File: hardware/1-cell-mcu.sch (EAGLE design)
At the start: 13 parts, among them IC1 PIC12LF1571, J1 ICSP_HEADER, J2 HEADER_4P, J3 HEADER_4P

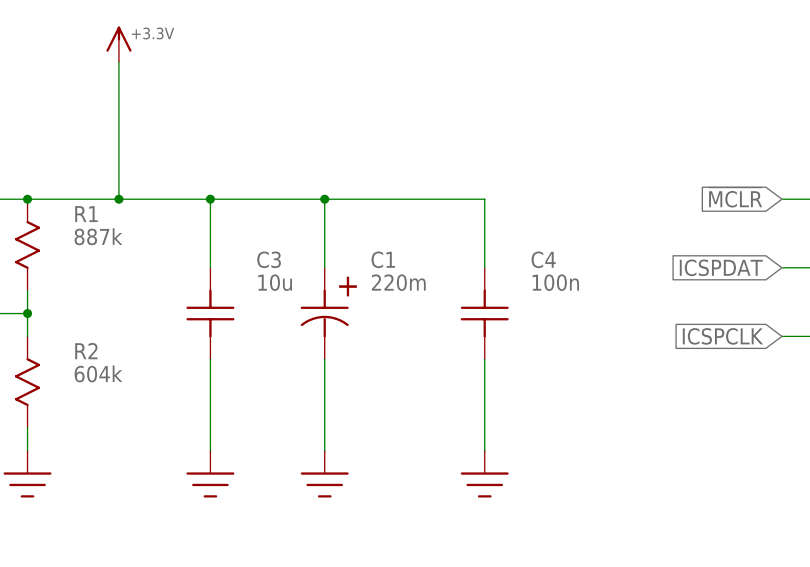
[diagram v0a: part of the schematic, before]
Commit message: updated supercap value
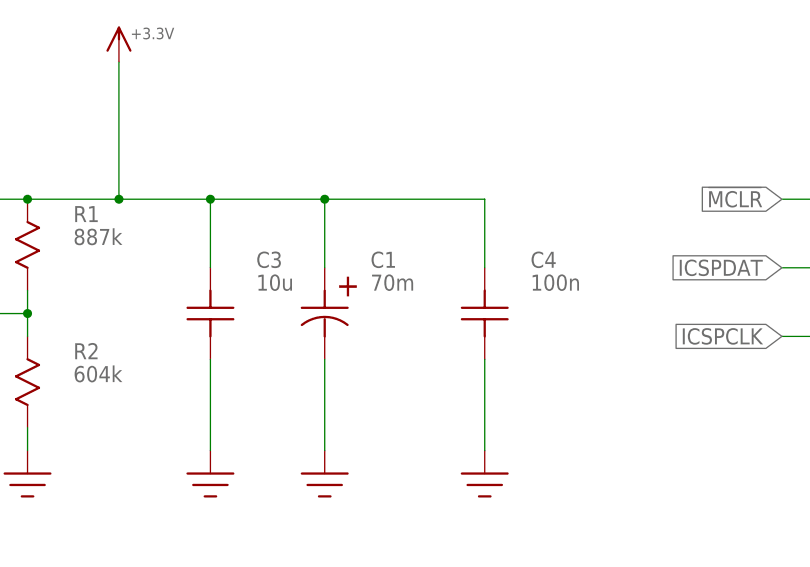
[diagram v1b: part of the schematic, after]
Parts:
- C1: value 220m -> 70m
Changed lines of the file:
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@@
 <part name="U$12" library="1-cell-mcu" deviceset="GND" device=""/>
 <part name="U$13" library="1-cell-mcu" deviceset="+3.3V" device=""/>
-<part name="C1" library="1-cell-mcu" deviceset="C_POL" device="" value="220m"/>
+<part name="C1" library="1-cell-mcu" deviceset="C_POL" device="" value="70m"/>
 <part name="C4" library="1-cell-mcu" deviceset="C" device="0805" value="100n"/>
 <part name="U$14" library="1-cell-mcu" deviceset="GND" device=""/>
